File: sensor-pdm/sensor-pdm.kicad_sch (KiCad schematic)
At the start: 2 parts, among them J1 Conn_01x04

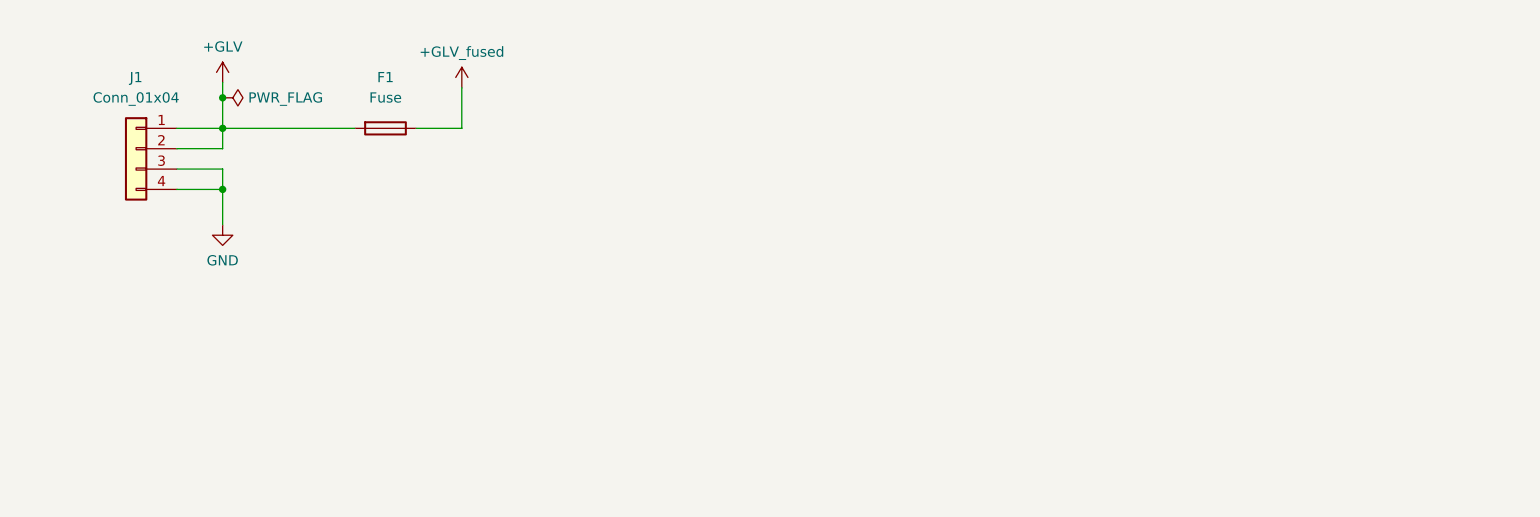
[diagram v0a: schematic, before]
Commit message: Added buck-boost schematic
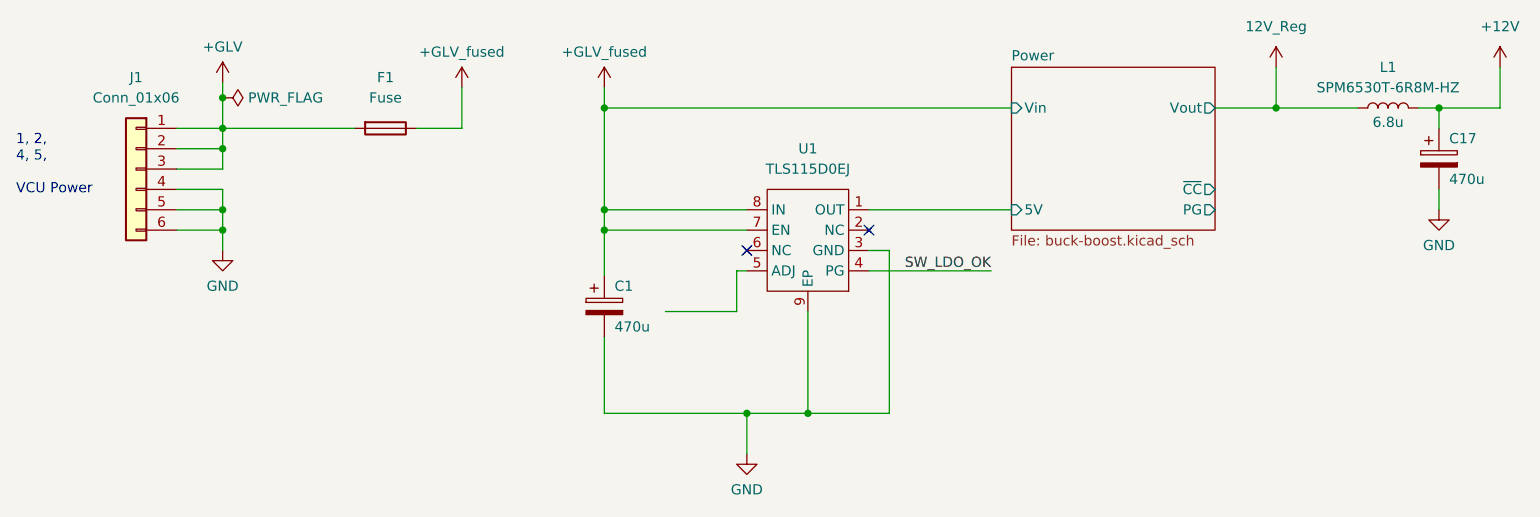
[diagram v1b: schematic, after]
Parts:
- added C1, C17: 470u, symbol Device:C_Polarized
- added L1: 6.8u, symbol Device:L
- added U1: TLS115D0EJ, Package_SO:Infineon_PG-DSO-8-27_3.9x4.9mm_EP2.65x3mm, symbol SUFST:TLS115D0EJ
- J1: value Conn_01x04 -> Conn_01x06; symbol Connector_Generic:Conn_01x04 -> Connector_Generic:Conn_01x06
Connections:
- net +GLV: now also J1.3 (Pin_3)
- net +GLV_fused: now also C1.1, U1.7 (EN), U1.8 (IN)
- net GND: now also J1.5 (Pin_5), J1.6 (Pin_6), C1.2, C17.2, U1.3 (GND), U1.9 (EP); no longer J1.3 (Pin_3)
- new net +12V: C17.1, L1.2
- new net 12V_Reg: L1.1
- new net Power/5V: U1.1 (OUT)
- new net SW_LDO_OK: U1.4 (PG)
- no-connect marks 0 -> 2
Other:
- added sheet Power (buck-boost.kicad_sch)
- note added: "1, 2, 4, 5, VCU Power"

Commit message: Via farms are a lie made by big drill to sell more drill bits
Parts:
- removed C1: 470u, symbol Device:C_Polarized
- removed U1: TLS115D0EJ, Package_SO:Infineon_PG-DSO-8-27_3.9x4.9mm_EP2.65x3mm, symbol SUFST:TLS115D0EJ
- added H1, H2, H4, H5: MountingHole, MountingHole:MountingHole_3.2mm_M3_DIN965_Pad_TopBottom, symbol Mechanical:MountingHole
- added H3: MountingHole_Pad, MountingHole:MountingHole_3.2mm_M3_Pad_Via, symbol Mechanical:MountingHole_Pad
- added J2: Conn_01x08, Connector_Molex:Molex_Micro-Fit_3.0_43045-0800_2x04_P3.00mm_Horizontal, symbol Connector_Generic:Conn_01x08
- C1: renamed from C17; footprint (none) -> Capacitor_THT:CP_Radial_D10.0mm_P5.00mm
- F1: value Fuse -> 3A; footprint (none) -> Fuse:Fuse_1206_3216Metric
- J1: footprint (none) -> Connector_Molex:Molex_Micro-Fit_3.0_43045-0600_2x03_P3.00mm_Horizontal
- L1: footprint (none) -> SamacSys:SPM6530
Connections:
- net +12V: now also J2.1 (Pin_1), J2.2 (Pin_2), J2.3 (Pin_3), J2.4 (Pin_4)
- net GND: now also H3.1, J2.5 (Pin_5), J2.6 (Pin_6), J2.7 (Pin_7), J2.8 (Pin_8)
- no-connect marks 2 -> 0
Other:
- added sheet Analogue Power (linear_regulator.kicad_sch)
- moved on the sheet: C1, L1

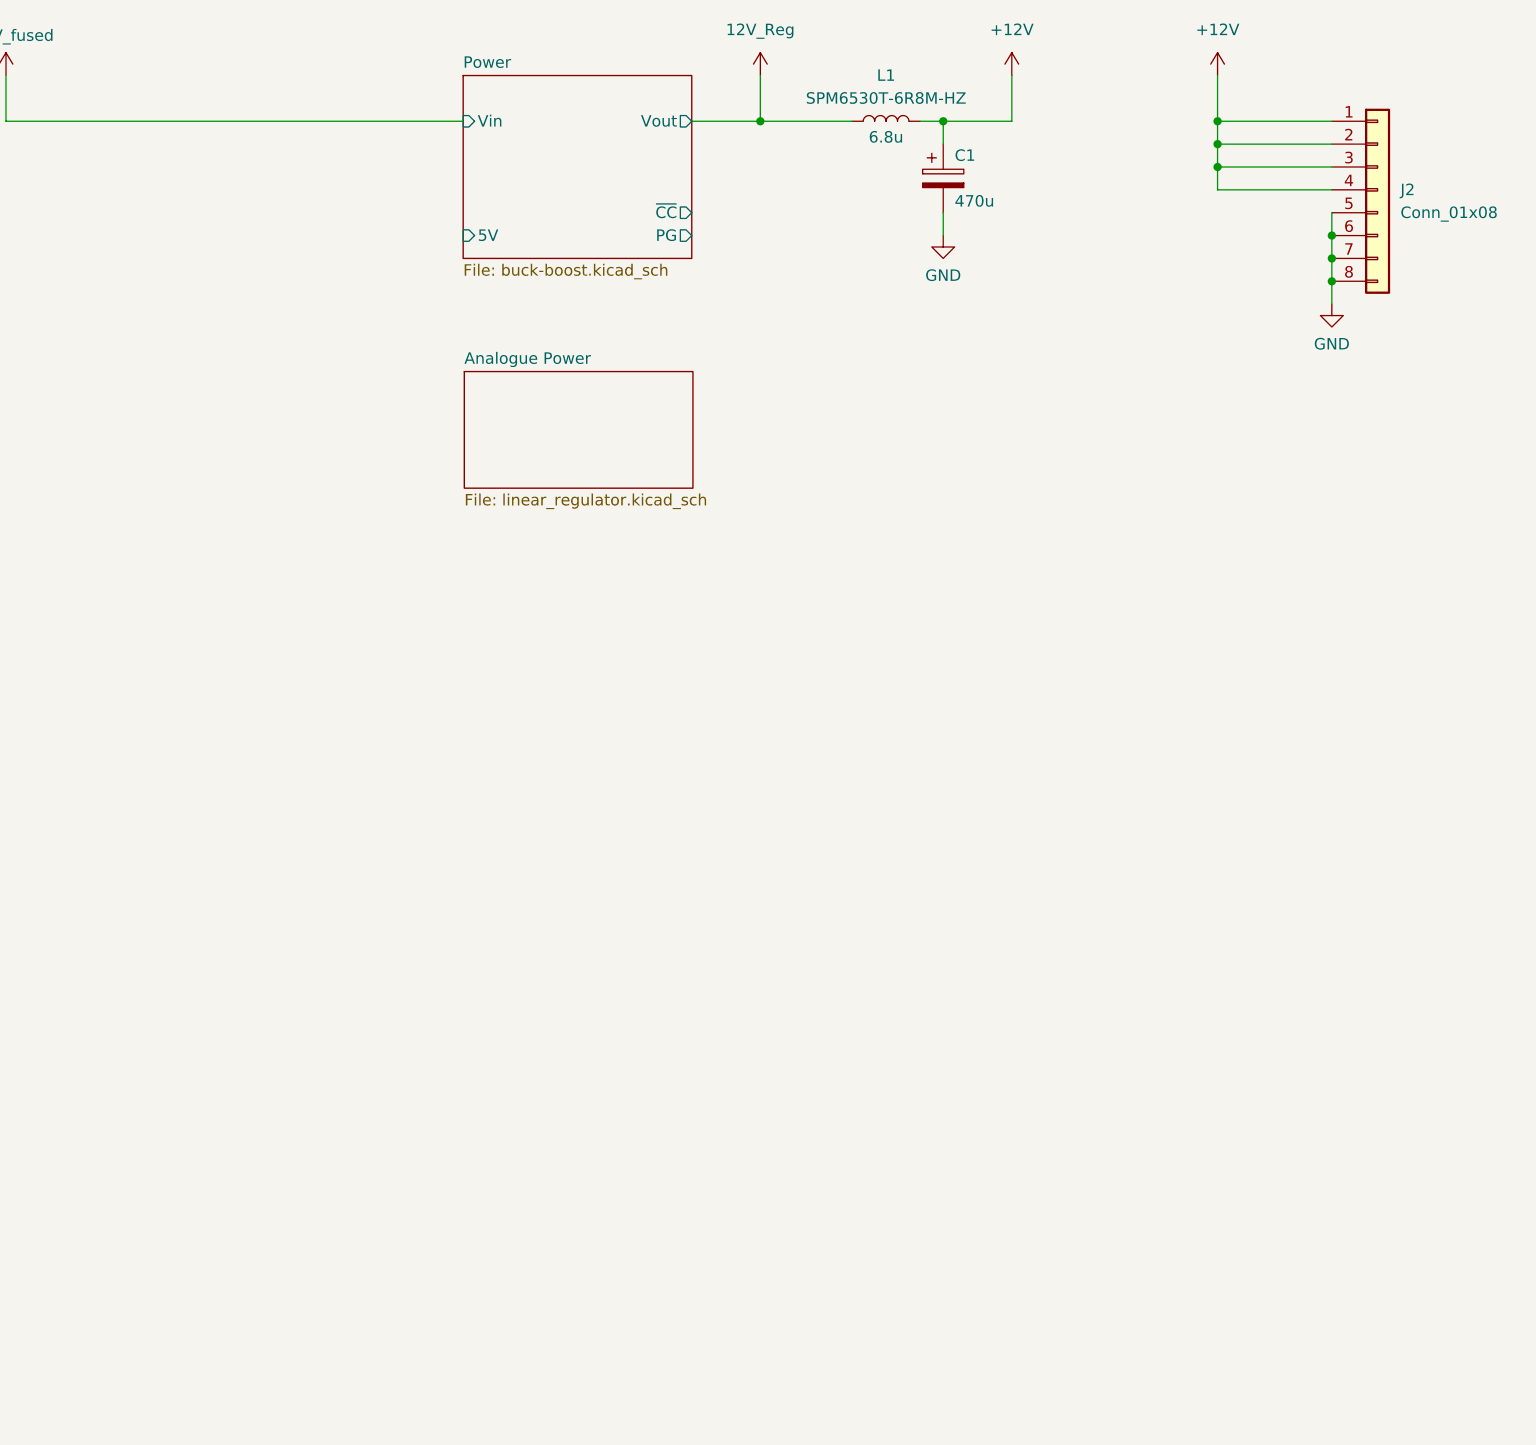
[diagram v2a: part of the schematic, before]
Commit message: Added sensor supply LDOs
TODO: See if LDOs are enough at dropout to handle switching noise
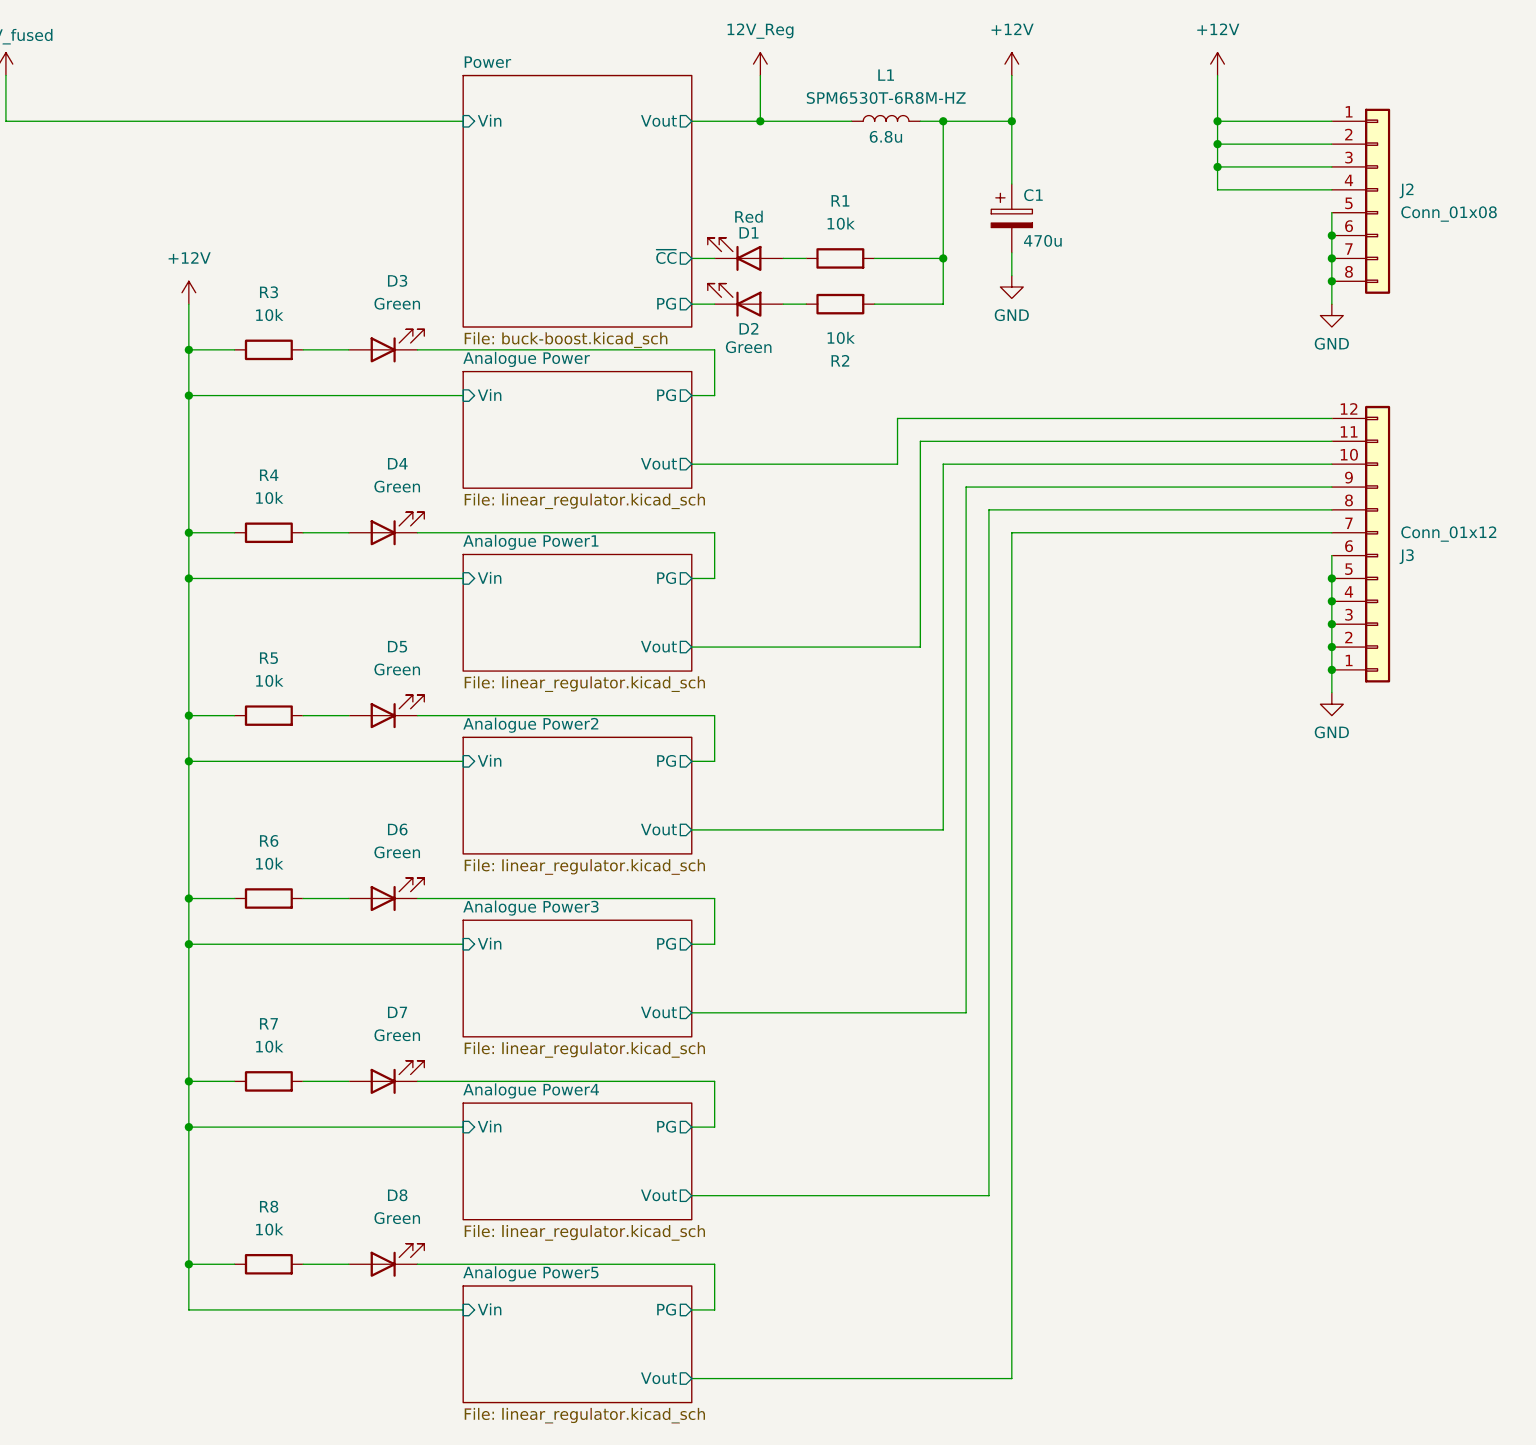
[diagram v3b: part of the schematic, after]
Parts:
- added D1: Red, LED_SMD:LED_0603_1608Metric, symbol Device:LED
- added D2, D3, D4, D5, D6, D7, D8: Green, LED_SMD:LED_0603_1608Metric, symbol Device:LED
- added J3: Conn_01x12, Connector_Molex:Molex_Micro-Fit_3.0_43045-1200_2x06_P3.00mm_Horizontal, symbol Connector_Generic:Conn_01x12
- added R1, R2, R3, R4, R5, R6, R7, R8: 10k, Resistor_SMD:R_0603_1608Metric, symbol Device:R
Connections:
- net +12V: now also R1.2, R2.2, R3.1, R4.1, R5.1, R6.1, R7.1, R8.1
- net GND: now also J3.1 (Pin_1), J3.2 (Pin_2), J3.3 (Pin_3), J3.4 (Pin_4), J3.5 (Pin_5), J3.6 (Pin_6)
- net Power/PG: now also D2.1 (K)
- net Power/~{CC}: now also D1.1 (K)
- new net: D3.2 (A), R3.2
- new net: D7.2 (A), R7.2
- new net: D1.2 (A), R1.1
- new net: D4.2 (A), R4.2
- new net: D8.2 (A), R8.2
- new net: D6.2 (A), R6.2
- new net: D2.2 (A), R2.1
- new net: D5.2 (A), R5.2
- new net Analogue Power/PG: D3.1 (K)
- new net Analogue Power/Vout: J3.12 (Pin_12)
- new net Analogue Power1/PG: D4.1 (K)
- new net Analogue Power1/Vout: J3.11 (Pin_11)
- new net Analogue Power2/PG: D5.1 (K)
- new net Analogue Power2/Vout: J3.10 (Pin_10)
- new net Analogue Power3/PG: D6.1 (K)
- new net Analogue Power3/Vout: J3.9 (Pin_9)
- new net Analogue Power4/PG: D7.1 (K)
- new net Analogue Power4/Vout: J3.8 (Pin_8)
- new net Analogue Power5/PG: D8.1 (K)
- new net Analogue Power5/Vout: J3.7 (Pin_7)
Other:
- added sheet Analogue Power1 (linear_regulator.kicad_sch)
- added sheet Analogue Power2 (linear_regulator.kicad_sch)
- added sheet Analogue Power3 (linear_regulator.kicad_sch)
- added sheet Analogue Power4 (linear_regulator.kicad_sch)
- added sheet Analogue Power5 (linear_regulator.kicad_sch)
- sheet Analogue Power ports: added PG, Vin, Vout; removed none
- sheet Power ports: added none; removed 5V
- moved on the sheet: C1

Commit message: Updated BOM, ready for review
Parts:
- C1: Mouser Part Number (none) -> 667-EEU-FR1V471; To Order (none) -> INV
- D1: Mouser Part Number (none) -> 755-SML-D12U1WT86; To Order (none) -> TRUE
- D2, D3, D4, D5, D6, D7, D8: Mouser Part Number (none) -> 755-SML-D12P8WT86; To Order (none) -> TRUE
- F1: value 3A -> 5A; footprint Fuse:Fuse_1206_3216Metric -> Fuse:Fuse_0603_1608Metric; Mouser Part Number (none) -> 603-JB06F5001R; To Order (none) -> TRUE
- H1, H2, H4, H5: footprint MountingHole:MountingHole_3.2mm_M3_DIN965_Pad_TopBottom -> MountingHole:MountingHole_3.2mm_M3_DIN965
- J1, J2, J3, L1: To Order (none) -> INV
- R1, R2, R3, R4, R5, R6, R7, R8: Mouser Part Number (none) -> 708-RNCP0603FTD10K0; To Order (none) -> INV

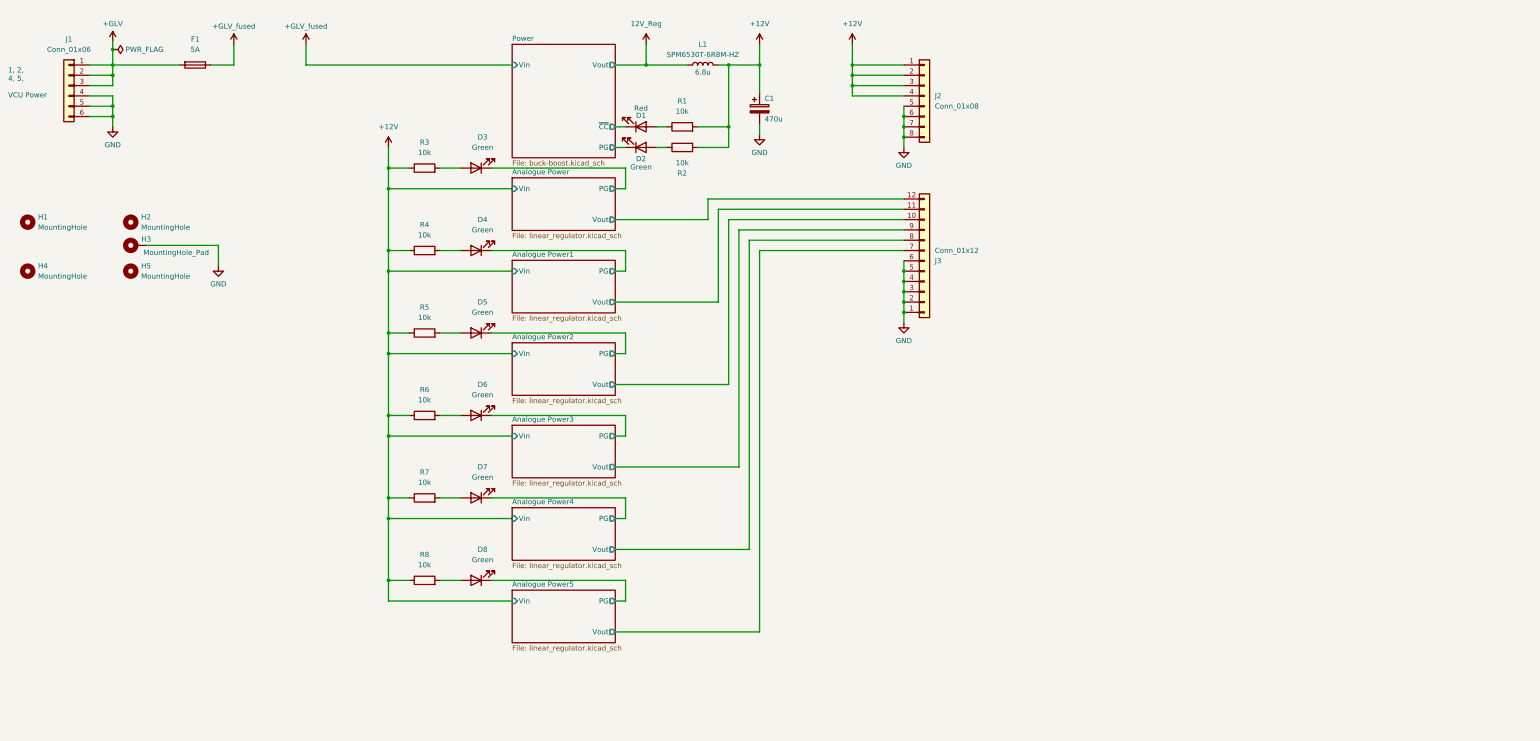
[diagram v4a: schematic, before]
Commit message: Implemented APPS SCS biasing
TODO: fusing buck-boost regulated output?
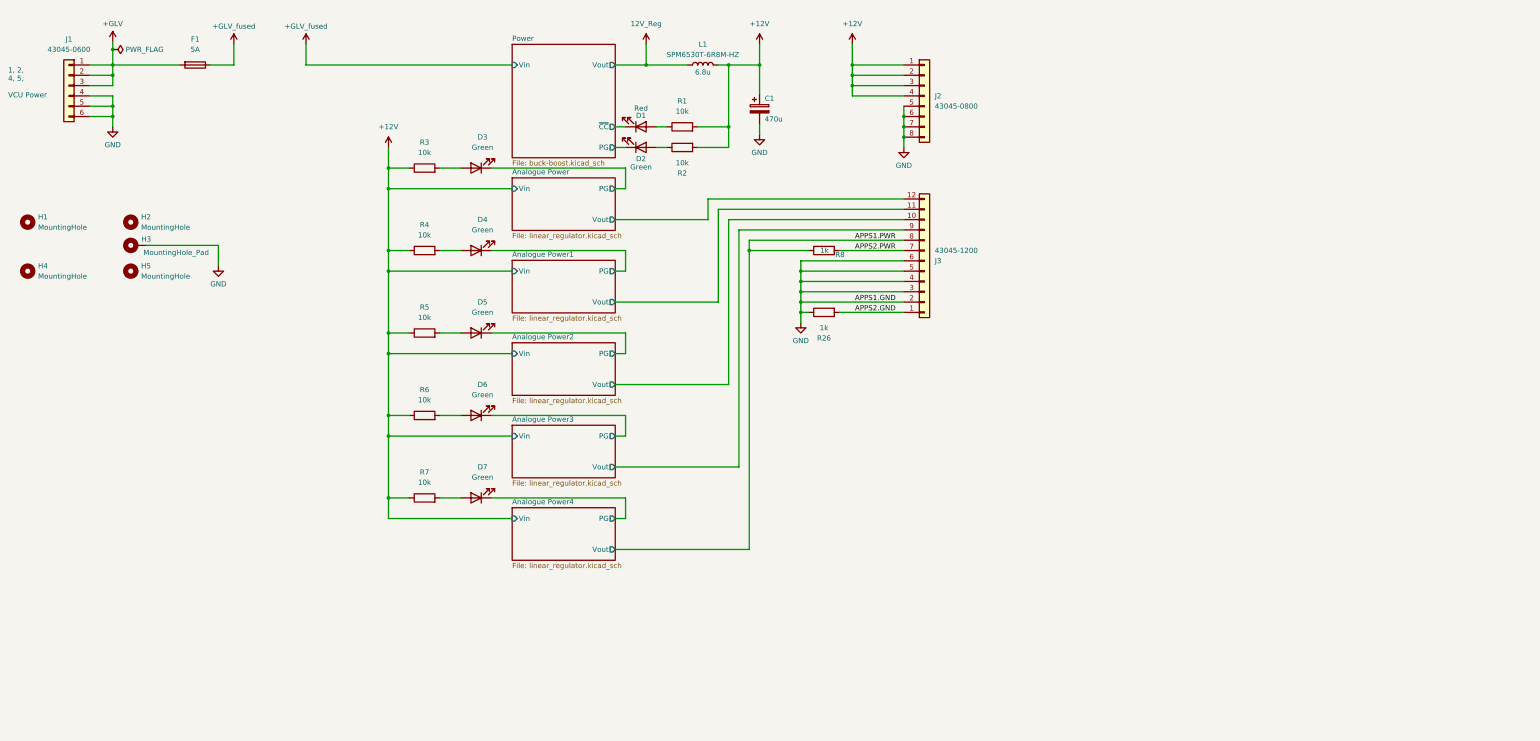
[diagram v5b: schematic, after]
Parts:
- removed D8: Green, LED_SMD:LED_0603_1608Metric, symbol Device:LED
- added R26: 1k, Resistor_SMD:R_0603_1608Metric, symbol Device:R
- J1: value Conn_01x06 -> 43045-0600
- J2: value Conn_01x08 -> 43045-0800
- J3: value Conn_01x12 -> 43045-1200
- R8: value 10k -> 1k
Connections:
- net Analogue Power5/Vout is gone; now on net APPS2.PWR: J3.7 (Pin_7)
- net +12V: no longer R8.1
- net GND: now also R26.1; no longer J3.1 (Pin_1)
- net APPS2.PWR: now reaches R8.2
- net Analogue Power4/Vout renamed APPS1.PWR
- net APPS1.PWR: now also R8.1
- new net APPS2.GND: J3.1 (Pin_1), R26.2
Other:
- removed sheet Analogue Power5
